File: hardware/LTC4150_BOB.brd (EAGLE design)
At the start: 15.2 x 30.5 mm, 23 parts, among them U1 LTC4150

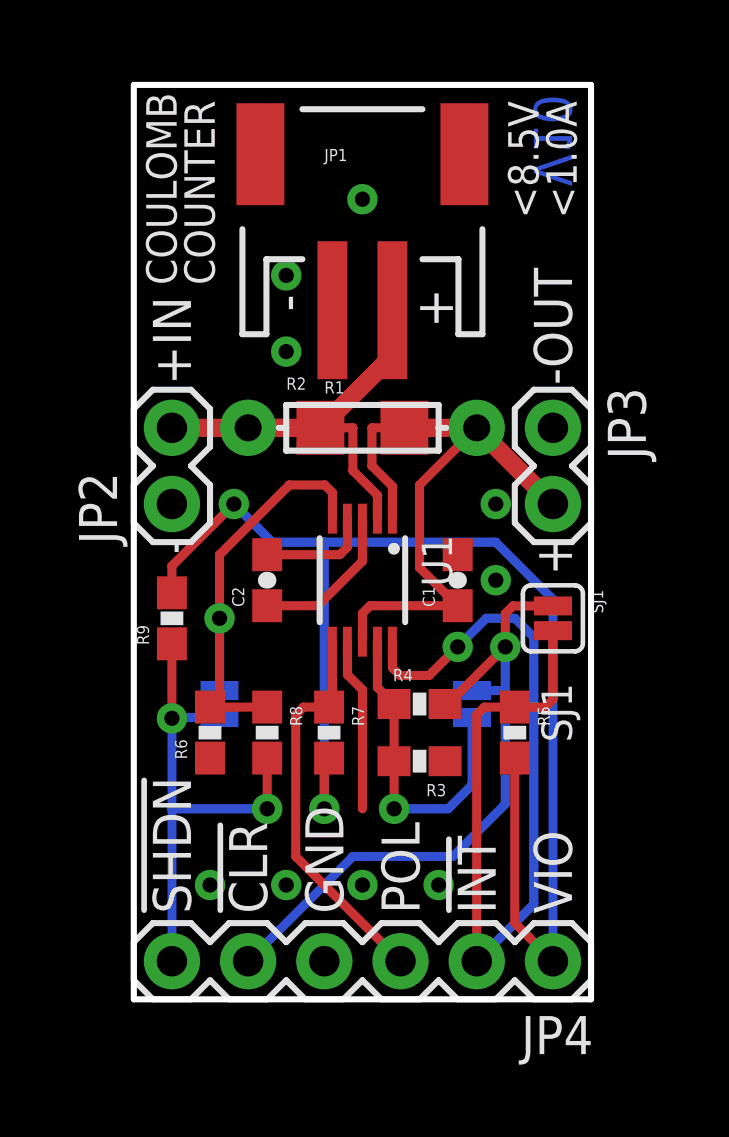
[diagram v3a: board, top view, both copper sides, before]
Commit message: added board fiducials
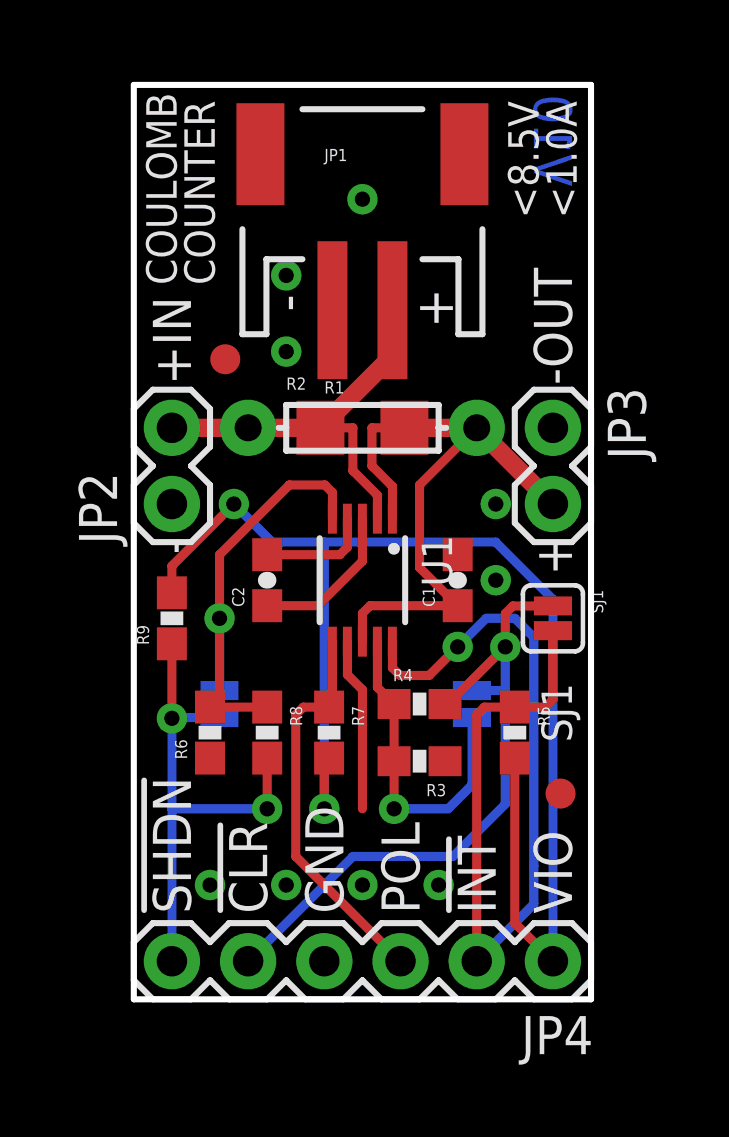
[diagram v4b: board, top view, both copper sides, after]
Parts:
- added FID1, FID2: FIDUCIAL1X2, SparkFun-Aesthetics:FIDUCIAL-1X2
